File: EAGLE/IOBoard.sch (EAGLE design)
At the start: 44 parts, among them IC1 TPS61097, Q1 8MHz, Q2 32kHz, U1 STM32F10XRXT6

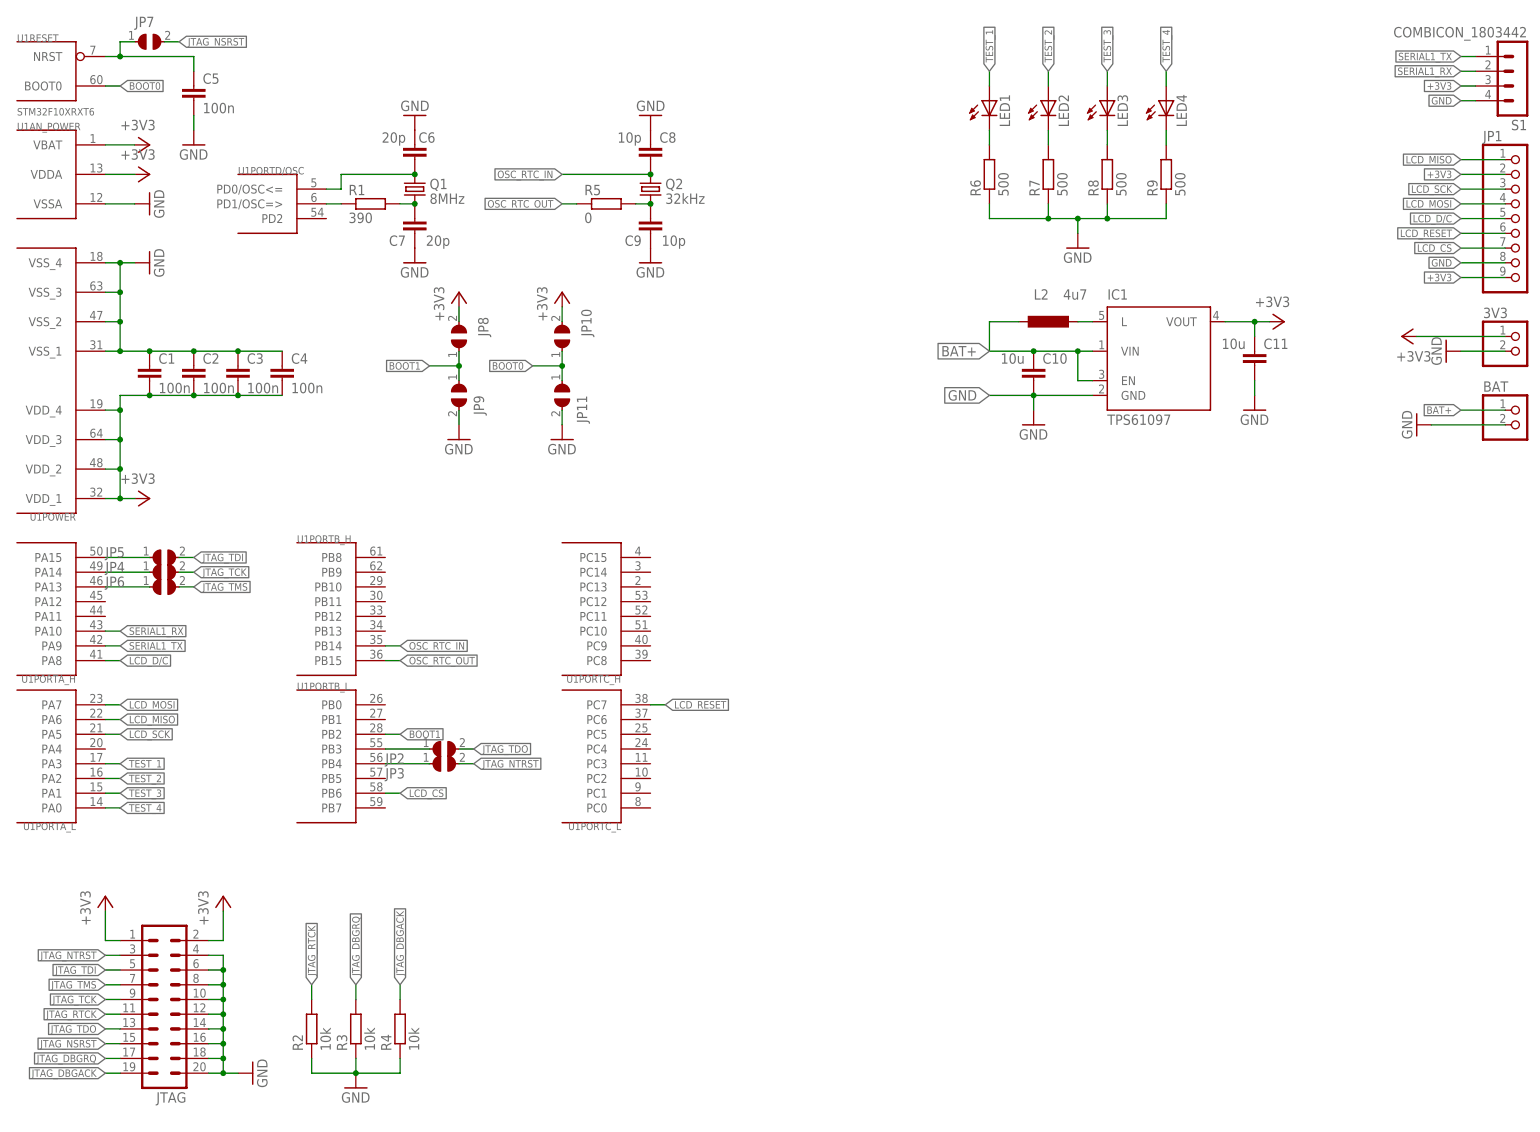
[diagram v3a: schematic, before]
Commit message: Finished first prototype of the circuit board
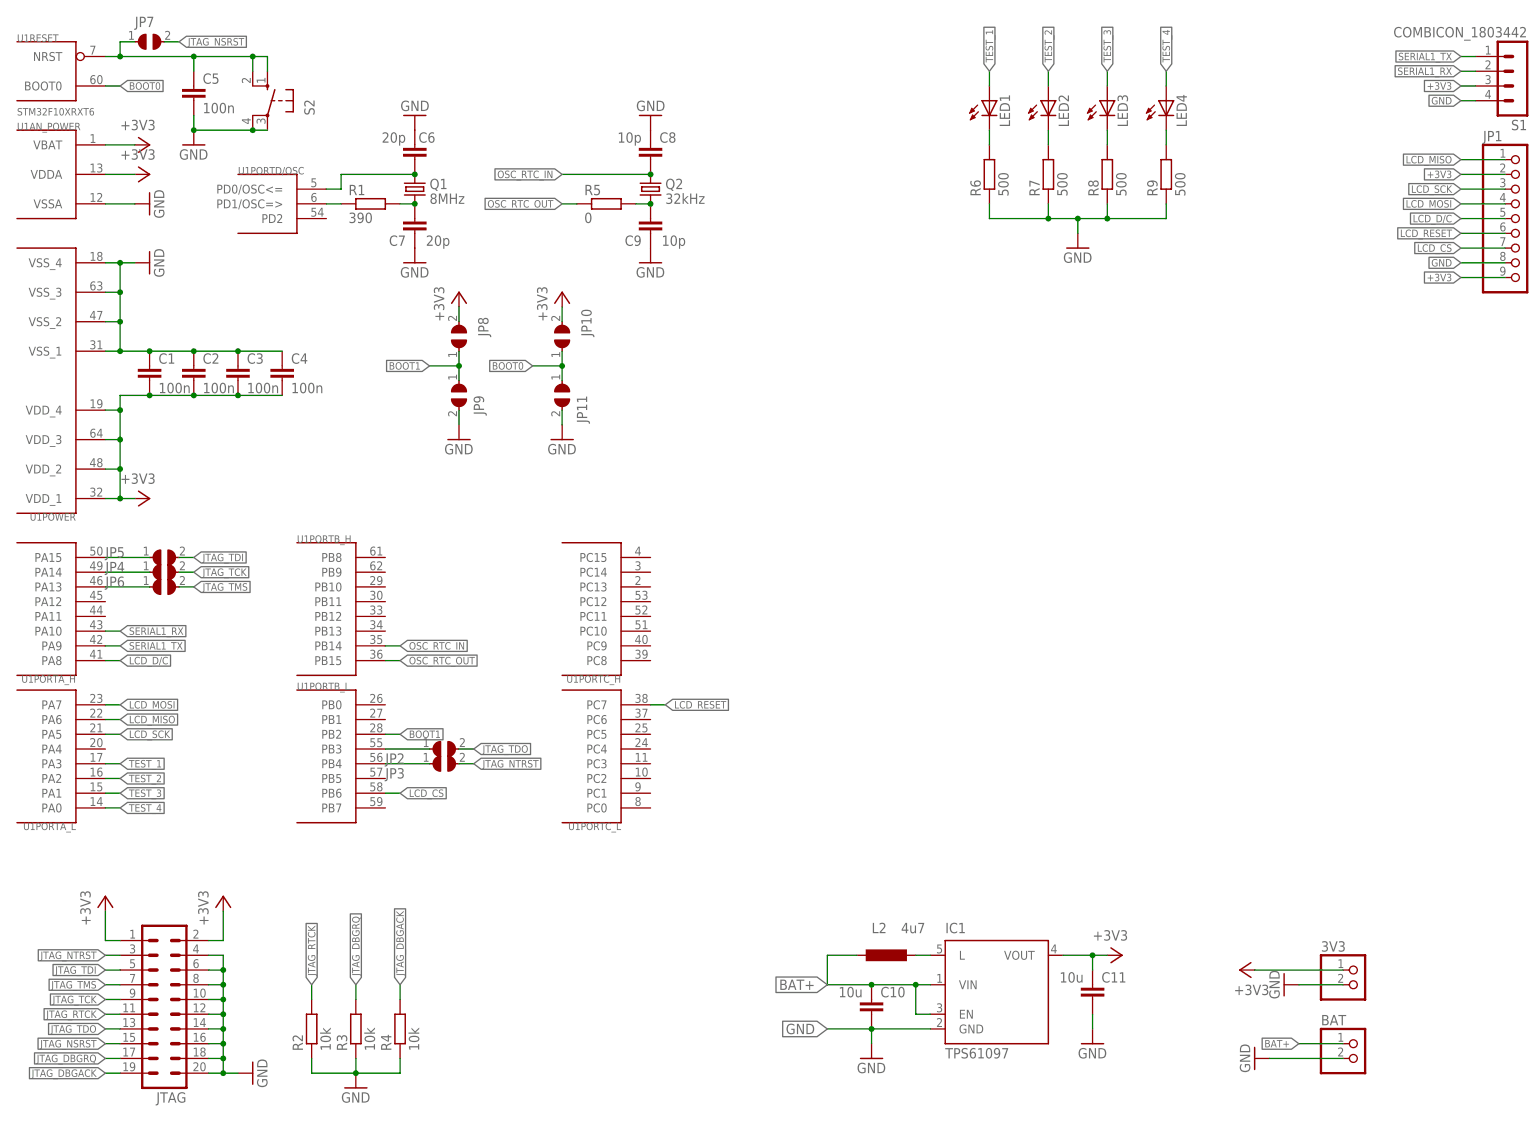
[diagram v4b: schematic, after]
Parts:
- added S2: (no value), switch-omron:10-XX
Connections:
- net GND: now also S2.P, S2.P1
- net N$1: now also S2.S, S2.S1
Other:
- note added: "Peripherals"
- note added: "Power Supply"
- moved on the sheet: 3V3, BAT, C10, C11, IC1, L2
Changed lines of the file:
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@@
 <?xml version="1.0" encoding="utf-8"?>
 <!DOCTYPE eagle SYSTEM "eagle.dtd">
-<eagle version="6.5.0">
+<eagle version="7.5.0">
 <drawing>
 <settings>
@@
 <part name="GND15" library="supply1" deviceset="GND" device=""/>
 <part name="GND16" library="supply1" deviceset="GND" device=""/>
+<part name="S2" library="switch-omron" deviceset="10-XX" device=""/>
 </parts>
 <sheets>
@@
 <wire x1="106.68" y1="129.54" x2="106.68" y2="134.62" width="0.254" layer="98"/>
 <wire x1="106.68" y1="134.62" x2="101.6" y2="134.62" width="0.254" layer="98"/>
+<wire x1="152.4" y1="50.8" x2="274.32" y2="50.8" width="1.27" layer="98"/>
+<text x="134.62" y="45.72" size="5.08" layer="98" rot="R180">Power Supply</text>
+<text x="271.78" y="60.96" size="5.08" layer="98" rot="R180">Peripherals</text>
 </plain>
 <instances>
@@
 <instance part="GND12" gate="1" x="104.14" y="124.46"/>
 <instance part="+3V7" gate="G$1" x="104.14" y="149.86"/>
-<instance part="3V3" gate="G$1" x="269.24" y="139.7"/>
-<instance part="GND13" gate="1" x="256.54" y="139.7" rot="R270"/>
-<instance part="+3V8" gate="G$1" x="248.92" y="142.24" rot="R90"/>
-<instance part="BAT" gate="G$1" x="269.24" y="127"/>
-<instance part="IC1" gate="G$1" x="205.74" y="137.16"/>
-<instance part="+3V9" gate="G$1" x="228.6" y="144.78" rot="R270"/>
-<instance part="L2" gate="G$1" x="187.96" y="144.78" smashed="yes">
-<attribute name="NAME" x="185.42" y="148.59" size="1.778" layer="95"/>
-<attribute name="VALUE" x="190.5" y="148.59" size="1.778" layer="96"/>
-</instance>
-<instance part="C10" gate="G$1" x="185.42" y="134.62" smashed="yes" rot="R180">
-<attribute name="NAME" x="186.944" y="137.541" size="1.778" layer="95"/>
-<attribute name="VALUE" x="183.896" y="139.319" size="1.778" layer="96" rot="R180"/>
-</instance>
-<instance part="C11" gate="G$1" x="223.52" y="137.16" smashed="yes" rot="R180">
-<attribute name="NAME" x="225.044" y="140.081" size="1.778" layer="95"/>
-<attribute name="VALUE" x="221.996" y="141.859" size="1.778" layer="96" rot="R180"/>
-</instance>
-<instance part="GND14" gate="1" x="223.52" y="129.54"/>
-<instance part="GND15" gate="1" x="185.42" y="127"/>
-<instance part="GND16" gate="1" x="251.46" y="127" rot="R270"/>
+<instance part="3V3" gate="G$1" x="241.3" y="30.48"/>
+<instance part="GND13" gate="1" x="228.6" y="30.48" rot="R270"/>
+<instance part="+3V8" gate="G$1" x="220.98" y="33.02" rot="R90"/>
+<instance part="BAT" gate="G$1" x="241.3" y="17.78"/>
+<instance part="IC1" gate="G$1" x="177.8" y="27.94"/>
+<instance part="+3V9" gate="G$1" x="200.66" y="35.56" rot="R270"/>
+<instance part="L2" gate="G$1" x="160.02" y="35.56" smashed="yes">
+<attribute name="NAME" x="157.48" y="39.37" size="1.778" layer="95"/>
+<attribute name="VALUE" x="162.56" y="39.37" size="1.778" layer="96"/>
+</instance>
+<instance part="C10" gate="G$1" x="157.48" y="25.4" smashed="yes" rot="R180">
+<attribute name="NAME" x="159.004" y="28.321" size="1.778" layer="95"/>
+<attribute name="VALUE" x="155.956" y="30.099" size="1.778" layer="96" rot="R180"/>
+</instance>
+<instance part="C11" gate="G$1" x="195.58" y="27.94" smashed="yes" rot="R180">
+<attribute name="NAME" x="197.104" y="30.861" size="1.778" layer="95"/>
+<attribute name="VALUE" x="194.056" y="32.639" size="1.778" layer="96" rot="R180"/>
+</instance>
+<instance part="GND14" gate="1" x="195.58" y="20.32"/>
+<instance part="GND15" gate="1" x="157.48" y="17.78"/>
+<instance part="GND16" gate="1" x="223.52" y="17.78" rot="R270"/>
+<instance part="S2" gate="1" x="53.34" y="182.88" rot="MR0"/>
 </instances>
 <busses>
@@
 <pinref part="C5" gate="G$1" pin="2"/>
 <wire x1="40.64" y1="177.8" x2="40.64" y2="180.34" width="0.1524" layer="91"/>
+<pinref part="S2" gate="1" pin="P1"/>
+<wire x1="50.8" y1="177.8" x2="40.64" y2="177.8" width="0.1524" layer="91"/>
+<junction x="40.64" y="177.8"/>
+<pinref part="S2" gate="1" pin="P"/>
+<wire x1="53.34" y1="177.8" x2="50.8" y2="177.8" width="0.1524" layer="91"/>
+<junction x="50.8" y="177.8"/>
 </segment>
 <segment>
@@
 <pinref part="3V3" gate="G$1" pin="2"/>
 <pinref part="GND13" gate="1" pin="GND"/>
-<wire x1="266.7" y1="139.7" x2="259.08" y2="139.7" width="0.1524" layer="91"/>
+<wire x1="238.76" y1="30.48" x2="231.14" y2="30.48" width="0.1524" layer="91"/>
 </segment>
 <segment>
 <pinref part="C11" gate="G$1" pin="1"/>
 <pinref part="GND14" gate="1" pin="GND"/>
-<wire x1="223.52" y1="134.62" x2="223.52" y2="132.08" width="0.1524" layer="91"/>
-</segment>
-<segment>
-<wire x1="195.58" y1="132.08" x2="185.42" y2="132.08" width="0.1524" layer="91"/>
+<wire x1="195.58" y1="25.4" x2="195.58" y2="22.86" width="0.1524" layer="91"/>
+</segment>
+<segment>
+<wire x1="167.64" y1="22.86" x2="157.48" y2="22.86" width="0.1524" layer="91"/>
 <pinref part="IC1" gate="G$1" pin="GND"/>
-<label x="177.8" y="132.08" size="1.778" layer="95" rot="R180" xref="yes"/>
+<label x="149.86" y="22.86" size="1.778" layer="95" rot="R180" xref="yes"/>
 <pinref part="C10" gate="G$1" pin="1"/>
-<wire x1="185.42" y1="132.08" x2="177.8" y2="132.08" width="0.1524" layer="91"/>
-<junction x="185.42" y="132.08"/>
+<wire x1="157.48" y1="22.86" x2="149.86" y2="22.86" width="0.1524" layer="91"/>
+<junction x="157.48" y="22.86"/>
 <pinref part="GND15" gate="1" pin="GND"/>
-<wire x1="185.42" y1="132.08" x2="185.42" y2="129.54" width="0.1524" layer="91"/>
+<wire x1="157.48" y1="22.86" x2="157.48" y2="20.32" width="0.1524" layer="91"/>
 </segment>
 <segment>
 <pinref part="BAT" gate="G$1" pin="2"/>
 <pinref part="GND16" gate="1" pin="GND"/>
-<wire x1="254" y1="127" x2="266.7" y2="127" width="0.1524" layer="91"/>
+<wire x1="226.06" y1="17.78" x2="238.76" y2="17.78" width="0.1524" layer="91"/>
 </segment>
 </net>
@@
 <pinref part="+3V8" gate="G$1" pin="+3V3"/>
 <pinref part="3V3" gate="G$1" pin="1"/>
-<wire x1="251.46" y1="142.24" x2="266.7" y2="142.24" width="0.1524" layer="91"/>
+<wire x1="223.52" y1="33.02" x2="238.76" y2="33.02" width="0.1524" layer="91"/>
 </segment>
 <segment>
 <pinref part="IC1" gate="G$1" pin="VOUT"/>
 <pinref part="+3V9" gate="G$1" pin="+3V3"/>
-<wire x1="218.44" y1="144.78" x2="223.52" y2="144.78" width="0.1524" layer="91"/>
+<wire x1="190.5" y1="35.56" x2="195.58" y2="35.56" width="0.1524" layer="91"/>
 <pinref part="C11" gate="G$1" pin="2"/>
-<wire x1="223.52" y1="144.78" x2="226.06" y2="144.78" width="0.1524" layer="91"/>
-<wire x1="223.52" y1="144.78" x2="223.52" y2="142.24" width="0.1524" layer="91"/>
-<junction x="223.52" y="144.78"/>
+<wire x1="195.58" y1="35.56" x2="198.12" y2="35.56" width="0.1524" layer="91"/>
+<wire x1="195.58" y1="35.56" x2="195.58" y2="33.02" width="0.1524" layer="91"/>
+<junction x="195.58" y="35.56"/>
 </segment>
 </net>
@@
 <wire x1="27.94" y1="193.04" x2="27.94" y2="190.5" width="0.1524" layer="91"/>
 <junction x="27.94" y="190.5"/>
+<pinref part="S2" gate="1" pin="S1"/>
+<wire x1="40.64" y1="190.5" x2="50.8" y2="190.5" width="0.1524" layer="91"/>
+<wire x1="50.8" y1="190.5" x2="50.8" y2="187.96" width="0.1524" layer="91"/>
+<junction x="40.64" y="190.5"/>
+<pinref part="S2" gate="1" pin="S"/>
+<wire x1="50.8" y1="190.5" x2="53.34" y2="190.5" width="0.1524" layer="91"/>
+<wire x1="53.34" y1="190.5" x2="53.34" y2="187.96" width="0.1524" layer="91"/>
+<junction x="50.8" y="190.5"/>
 </segment>
 </net>
@@
 <segment>
 <pinref part="BAT" gate="G$1" pin="1"/>
-<wire x1="266.7" y1="129.54" x2="259.08" y2="129.54" width="0.1524" layer="91"/>
-<label x="259.08" y="129.54" size="1.27" layer="95" rot="R180" xref="yes"/>
-</segment>
-<segment>
-<wire x1="195.58" y1="139.7" x2="193.04" y2="139.7" width="0.1524" layer="91"/>
+<wire x1="238.76" y1="20.32" x2="231.14" y2="20.32" width="0.1524" layer="91"/>
+<label x="231.14" y="20.32" size="1.27" layer="95" rot="R180" xref="yes"/>
+</segment>
+<segment>
+<wire x1="167.64" y1="30.48" x2="165.1" y2="30.48" width="0.1524" layer="91"/>
 <pinref part="IC1" gate="G$1" pin="VIN"/>
-<wire x1="193.04" y1="139.7" x2="193.04" y2="134.62" width="0.1524" layer="91"/>
-<junction x="193.04" y="139.7"/>
+<wire x1="165.1" y1="30.48" x2="165.1" y2="25.4" width="0.1524" layer="91"/>
+<junction x="165.1" y="30.48"/>
 <pinref part="IC1" gate="G$1" pin="EN"/>
-<wire x1="193.04" y1="134.62" x2="195.58" y2="134.62" width="0.1524" layer="91"/>
-<label x="177.8" y="139.7" size="1.778" layer="95" rot="R180" xref="yes"/>
-<wire x1="193.04" y1="139.7" x2="185.42" y2="139.7" width="0.1524" layer="91"/>
+<wire x1="165.1" y1="25.4" x2="167.64" y2="25.4" width="0.1524" layer="91"/>
+<label x="149.86" y="30.48" size="1.778" layer="95" rot="R180" xref="yes"/>
+<wire x1="165.1" y1="30.48" x2="157.48" y2="30.48" width="0.1524" layer="91"/>
 <pinref part="L2" gate="G$1" pin="1"/>
-<wire x1="185.42" y1="139.7" x2="177.8" y2="139.7" width="0.1524" layer="91"/>
-<wire x1="182.88" y1="144.78" x2="177.8" y2="144.78" width="0.1524" layer="91"/>
-<wire x1="177.8" y1="144.78" x2="177.8" y2="139.7" width="0.1524" layer="91"/>
+<wire x1="157.48" y1="30.48" x2="149.86" y2="30.48" width="0.1524" layer="91"/>
+<wire x1="154.94" y1="35.56" x2="149.86" y2="35.56" width="0.1524" layer="91"/>
+<wire x1="149.86" y1="35.56" x2="149.86" y2="30.48" width="0.1524" layer="91"/>
 <pinref part="C10" gate="G$1" pin="2"/>
-<junction x="185.42" y="139.7"/>
+<junction x="157.48" y="30.48"/>
 </segment>
 </net>
@@
 <pinref part="IC1" gate="G$1" pin="L"/>
 <pinref part="L2" gate="G$1" pin="2"/>
-<wire x1="195.58" y1="144.78" x2="193.04" y2="144.78" width="0.1524" layer="91"/>
-</segment>
-</net>
+<wire x1="167.64" y1="35.56" x2="165.1" y2="35.56" width="0.1524" layer="91"/>
+</segment>
+</net>
